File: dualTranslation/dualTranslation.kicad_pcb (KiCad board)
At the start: 4 copper layers, 39.4 x 39.2 mm, 57 parts, among them IC1 LSF0108PWR, IC2 LSF0108PWR, IC3 TLV61225DC, J1 L_dual, J2 R_dual, J6 MISC

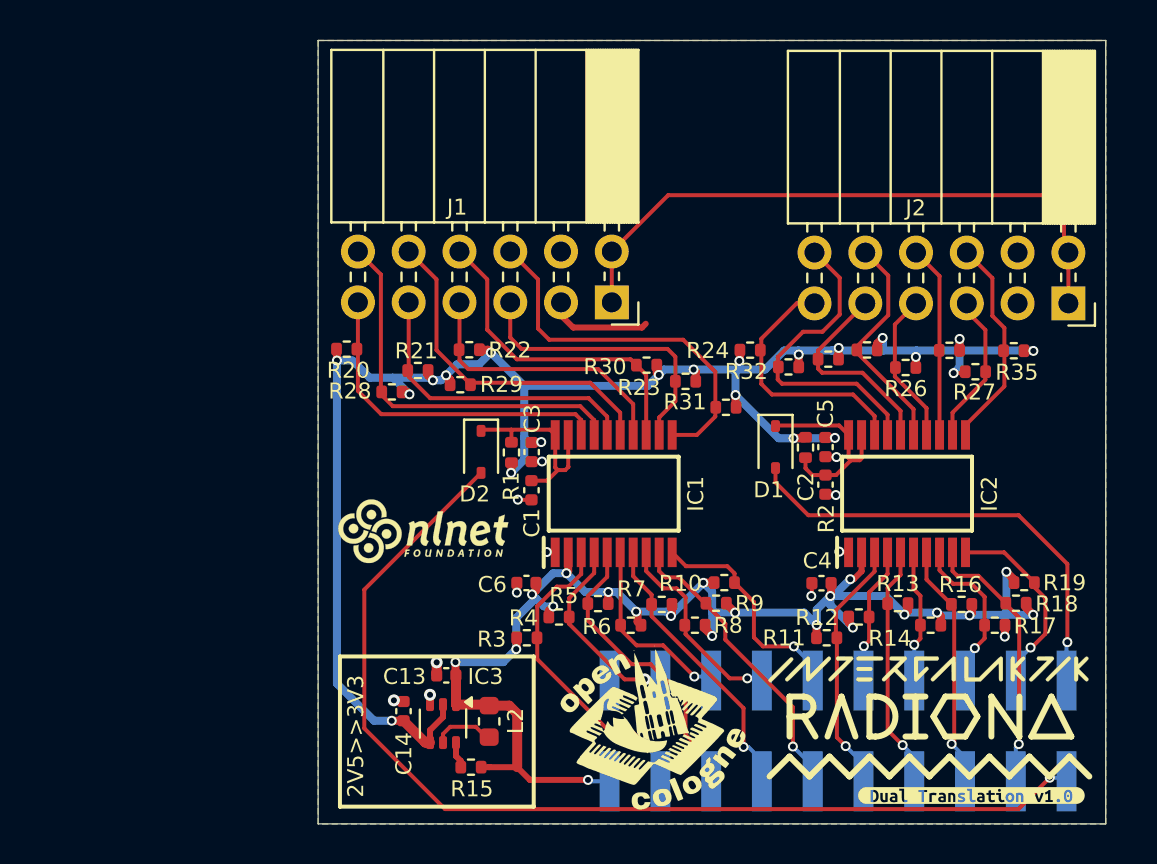
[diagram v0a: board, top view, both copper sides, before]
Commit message: Adding transistor
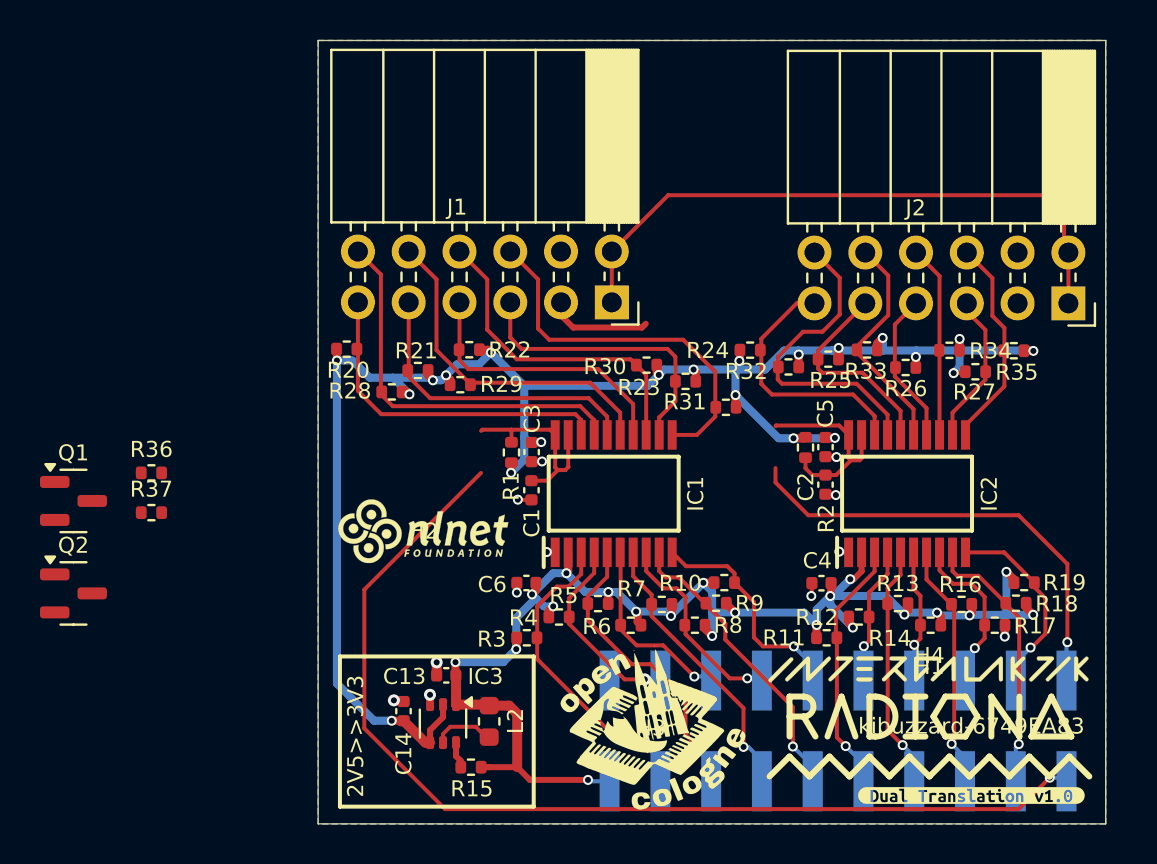
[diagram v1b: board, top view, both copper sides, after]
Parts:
- removed D1, D2: RB751V40T1G, Diode_SMD:D_SOD-323
- added Q1: MMBT3904, Package_TO_SOT_SMD:SOT-23, F.Cu at (95.0, 91.5)
- added Q2: MMBT3904, Package_TO_SOT_SMD:SOT-23, F.Cu at (95.0, 96.1)
- added R36: 2K, Resistor_SMD:R_0402_1005Metric, F.Cu at (98.9, 90.1)
- added R37: 2K, Resistor_SMD:R_0402_1005Metric, F.Cu at (98.9, 92.1)
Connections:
- C1 pad 1: Net-(D2-K) -> Net-(Q1-E)
- C2 pad 1: Net-(D1-K) -> Net-(Q2-E)
- IC1 pad 19: Net-(D2-K) -> Net-(IC1-EN)
- IC1 pad 20: Net-(D2-K) -> Net-(IC1-EN)
- IC2 pad 19: Net-(D1-K) -> Net-(IC2-EN)
- IC2 pad 20: Net-(D1-K) -> Net-(IC2-EN)
- R1 pad 2: Net-(D2-K) -> Net-(IC1-EN)
- R2 pad 2: Net-(D1-K) -> Net-(IC2-EN)
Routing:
- net (no net): track 0.00 -> 20.2 mm
- net Net-(D1-K): track 10.2 -> 0.00 mm
- net Net-(D2-K): track 10.0 -> 0.00 mm

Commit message: Routing
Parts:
- moved Q2 34.1 mm to (128.5, 89.7)
- moved R37 32.0 mm to (130.8, 92.2), turned to 180 degrees
- moved Q1 19.7 mm to (114.6, 90.0), turned to 90 degrees
- moved R36 12.8 mm to (109.5, 97.2), turned to 90 degrees
- moved R2 0.63 mm to (131.0, 88.9)
- moved R26 0.39 mm to (136.9, 85.0)
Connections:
- C1 pad 1: Net-(Q1-E) -> Net-(IC1-EN)
- C2 pad 1: Net-(Q2-E) -> GND
- C2 pad 2: GND -> Net-(IC2-EN)
- Q1 pad 2: Net-(Q1-E) -> GND
- Q2 pad 2: Net-(Q2-E) -> GND
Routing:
- net (no net): track 20.2 -> 0.00 mm
- net Net-(IC1-EN): track 0.00 -> 11.7 mm
- net Net-(IC2-EN): track 0.00 -> 11.0 mm
- net /NB_A8: track 52.7 -> 42.7 mm
- net Net-(Q2-B): track 0.00 -> 7.73 mm
- net Net-(Q1-B): track 0.00 -> 7.46 mm
- net /NB_B8: track 22.9 -> 20.2 mm
- net GND: track 11.3 -> 12.8 mm, vias 11 -> 58
- net +3V3: track 90.6 -> 91.9 mm
